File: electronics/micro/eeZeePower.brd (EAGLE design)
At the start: 20.3 x 11.6 mm, 10 parts

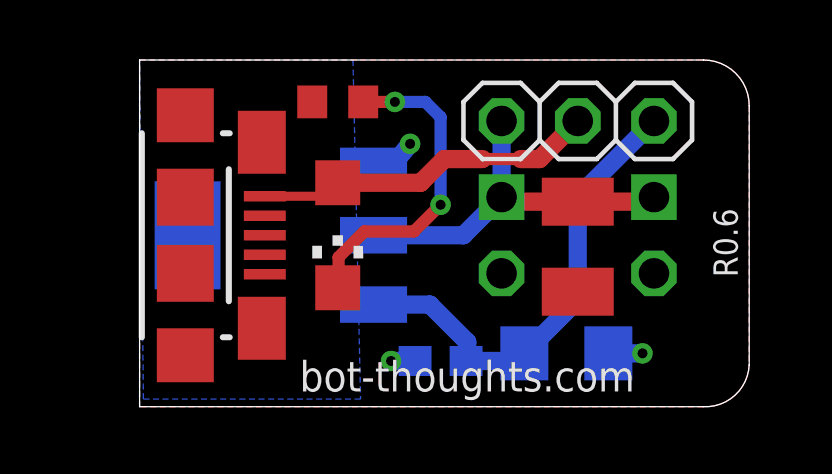
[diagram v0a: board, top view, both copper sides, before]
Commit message: microb: replaced usb micro b connector symbol & footprint
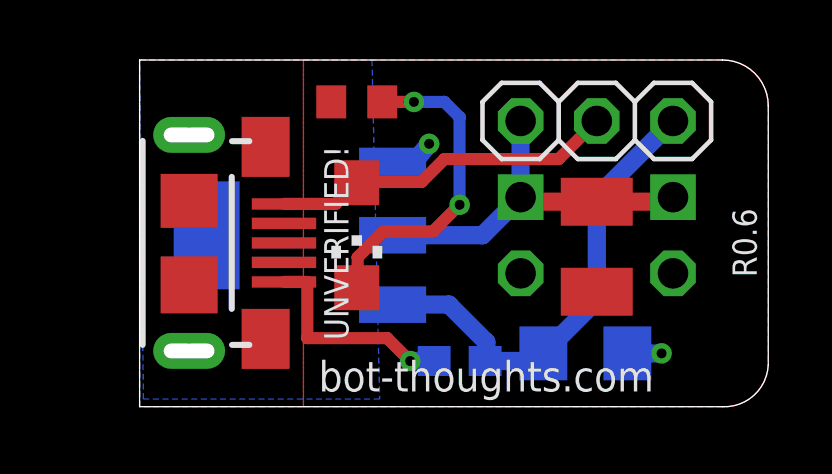
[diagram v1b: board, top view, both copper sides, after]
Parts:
- removed JP1: USB-MICROB, bt_electromech:USB-MICROB
- added X1: USB-MICROB, bt_electromech:USB-MICROB-4
- moved JP4 0.64 mm to (17.8, 5.71)
- moved C1 0.63 mm to (14.9, 1.78)
- moved C2 0.63 mm to (10.7, 1.52)
- moved C4 0.63 mm to (15.2, 5.33)
- moved JP10 0.63 mm to (15.2, 9.53)
- moved JP3 0.63 mm to (12.7, 5.71)
- moved LED1 0.63 mm to (7.24, 5.71)
- moved R1 0.63 mm to (7.24, 10.2)
- moved U1 0.63 mm to (5.33, 5.71)
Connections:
- new net SHIELD: X1.SHIELD1, X1.SHIELD2, X1.SHIELD3, X1.SHIELD4, X1.SHIELD5, X1.SHIELD6
- net GND: now also X1.GND; no longer JP1.GND, JP1.MT1, JP1.MT2, JP1.MT3, JP1.MT4
- net VBUS: now also X1.VBUS; no longer JP1.VBUS
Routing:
- net GND: track 3.51 -> 9.90 mm
- net VBUS: track 11.5 -> 12.2 mm
- added copper zone on layer 1, net SHIELD
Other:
- board size 20.3 x 11.6 mm -> 21 x 11.6 mm

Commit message: layout tweak, shrink board width, fix gnd pour connection
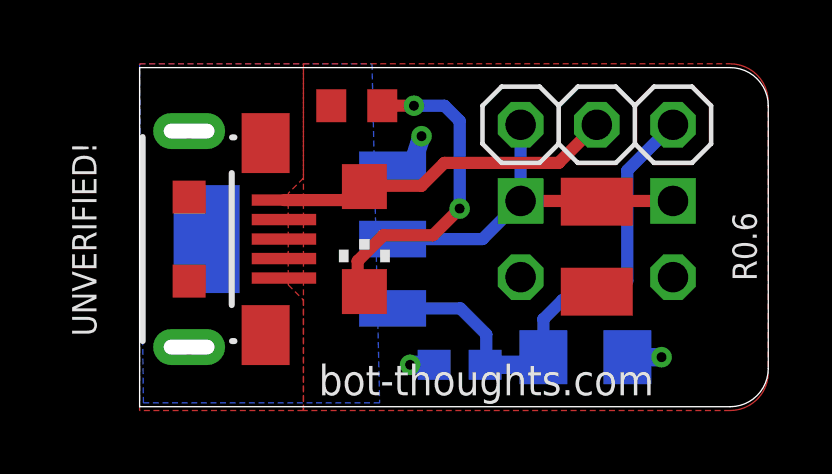
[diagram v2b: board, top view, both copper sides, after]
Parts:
- moved LED1 0.28 mm to (7.49, 5.59)
- moved JP10 0.13 mm to (15.2, 9.40)
- moved R1 0.13 mm to (7.24, 10.0)
- moved C1 0.13 mm to (14.9, 1.65)
- moved C2 0.13 mm to (10.7, 1.40)
- moved JP3 0.13 mm to (12.7, 5.59)
- moved JP4 0.13 mm to (17.8, 5.59)
- moved U1 0.13 mm to (5.33, 5.59)
- moved X1 0.13 mm to (1.65, 5.59)
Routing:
- net GND: track 9.90 -> 3.72 mm
- net VIN: track 15.9 -> 17.0 mm
- net VBUS: track 12.2 -> 12.8 mm
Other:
- board size 21 x 11.6 mm -> 21 x 11.3 mm
